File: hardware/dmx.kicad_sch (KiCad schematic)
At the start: 38 parts, among them J101 CORTEX-DEBUG, J102 JAE_DX07S016JA3, SW101 SW_Push, SW102 SW_Push, U101 TPS78433QWDRBRQ1, U102 ATSAMD51G, Y101 32k768

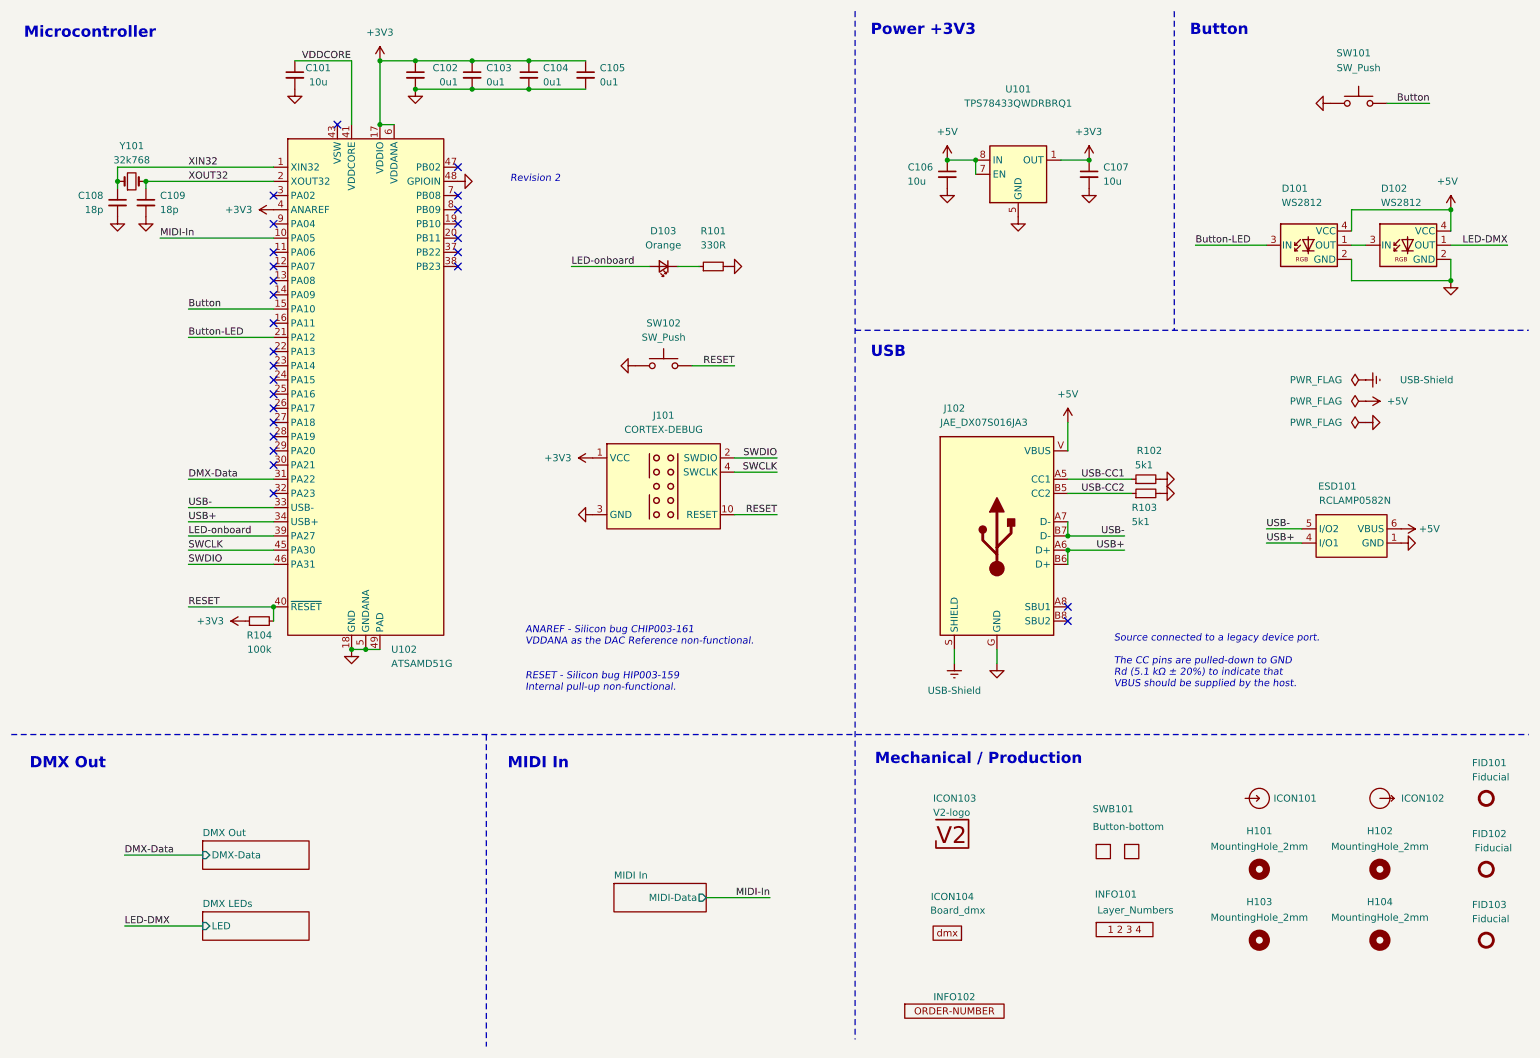
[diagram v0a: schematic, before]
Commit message: Update symbols
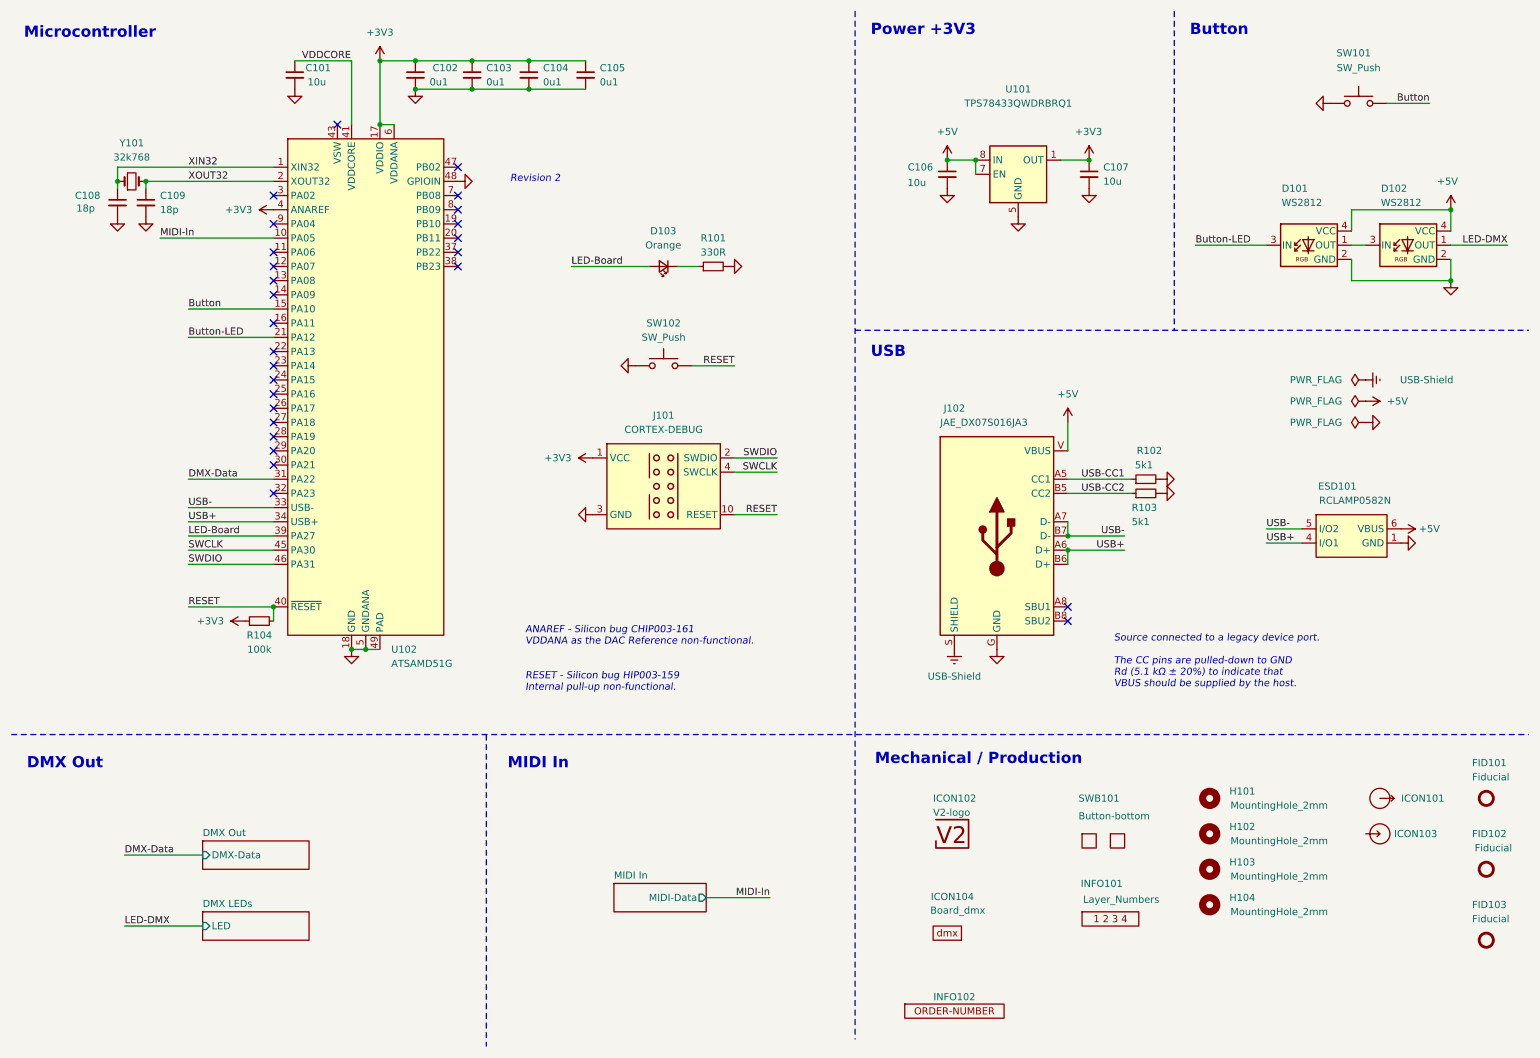
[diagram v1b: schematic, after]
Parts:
- C101: footprint Capacitor_SMD:C_0603_1608Metric -> V2_Capacitor_SMD:C_0603; symbol Device:C_Small -> V2_Device:C_0603_10u; Mouser (none) -> 810-C1608X6S1A106M
- C102, C103, C104, C105: footprint Capacitor_SMD:C_0603_1608Metric -> V2_Capacitor_SMD:C_0603; symbol Device:C_Small -> V2_Device:C_0603_0u1; Mouser (none) -> 810-CGA3E2X7R1H104MA
- C106, C107: footprint Capacitor_SMD:C_0603_1608Metric -> V2_Capacitor_SMD:C_0805; symbol Device:C_Small -> V2_Device:C_0805_10u; Mouser (none) -> 810-C2012X5R1E106K
- C108, C109: footprint Capacitor_SMD:C_0603_1608Metric -> V2_Capacitor_SMD:C_0603; symbol Device:C_Small -> V2_Device:C_0603_18p; Mouser (none) -> 603-CC603JRNPO9BN180
- D103: footprint LED_SMD:LED_0603_1608Metric -> V2_LED:LED_0603; symbol Device:LED_Small -> V2_Device:LED_0603_Orange; Mouser (none) -> 755-SML-D12M8WT86C
- ESD101: Mouser (none) -> 947-RCLAMP0582N.TCT
- J102: Mouser (none) -> 656-DX07S016JA3R1500
- R101: footprint Resistor_SMD:R_0603_1608Metric -> V2_Resistor_SMD:R_0603; symbol Device:R_Small -> V2_Device:R_0603_330R; Mouser (none) -> 71-CRCW0603330RFKEAC
- R102, R103: footprint Resistor_SMD:R_0603_1608Metric -> V2_Resistor_SMD:R_0603; symbol Device:R_Small -> V2_Device:R_0603_5k1; Mouser (none) -> 71-CRCW06035K10FKEAC
- R104: footprint Resistor_SMD:R_0603_1608Metric -> V2_Resistor_SMD:R_0603; symbol Device:R_Small -> V2_Device:R_0603_100k; Mouser (none) -> 71-CRCW0603100KFKEAC
- SW101, SW102: symbol Switch:SW_Push -> V2_Switch:SKSG; Mouser (none) -> 688-SKSGACE010
- U101: Mouser (none) -> 595-TPS78433QWDRBRQ1
- U102: Mouser (none) -> 556-ATSAMD51G19AMU
- Y101: symbol Device:Crystal_Small -> V2_Device:Crystal_3.2x1.5_32k768; Mouser (none) -> 815-ABS0716632.768KT
- renumbered H103 to H102, H102 to H103, ICON102 to ICON101, ICON103 to ICON102, ICON101 to ICON103
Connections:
- net LED-onboard renamed LED-Board
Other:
- moved on the sheet: H101, H102, H103, H104, ICON103, INFO101, SWB101

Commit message: Refresh
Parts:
- C101: Mouser 810-C1608X6S1A106M -> 810-C1608X6S1A106M
- C102, C103, C104, C105: Mouser 810-CGA3E2X7R1H104MA -> 810-CGA3E2X7R1H104MA
- C106, C107: footprint V2_Capacitor_SMD:C_0805 -> V2_Capacitor_SMD:C_0603; Mouser 810-C2012X5R1E106K -> 810-C2012X5R1E106K
- C108, C109: Mouser 603-CC603JRNPO9BN180 -> 603-CC603JRNPO9BN180
- D103: Mouser 755-SML-D12M8WT86C -> 755-SML-D12M8WT86C
- FID101, FID102, FID103: value Fiducial -> Fiducial_Paste
- INFO102: value ORDER-NUMBER -> Order_Number
- J101: value CORTEX-DEBUG -> Cortex_Debug
- J102: value JAE_DX07S016JA3 -> DX07S016JA3; Mouser 656-DX07S016JA3R1500 -> 656-DX07S016JA3R1500
- R101: Mouser 71-CRCW0603330RFKEAC -> 71-CRCW0603330RFKEAC
- R102, R103: Mouser 71-CRCW06035K10FKEAC -> 71-CRCW06035K10FKEAC
- R104: Mouser 71-CRCW0603100KFKEAC -> 71-CRCW0603100KFKEAC
- SW101, SW102: value SW_Push -> SKSG; Mouser 688-SKSGACE010 -> 688-SKSGACE010
- Y101: Mouser 815-ABS0716632.768KT -> 815-ABS0716632.768KT
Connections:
- net USB-Shield renamed Earth
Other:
- moved on the sheet: FID101, FID102, FID103, H101, H102, H103, H104, ICON101, ICON103, INFO101, SWB101

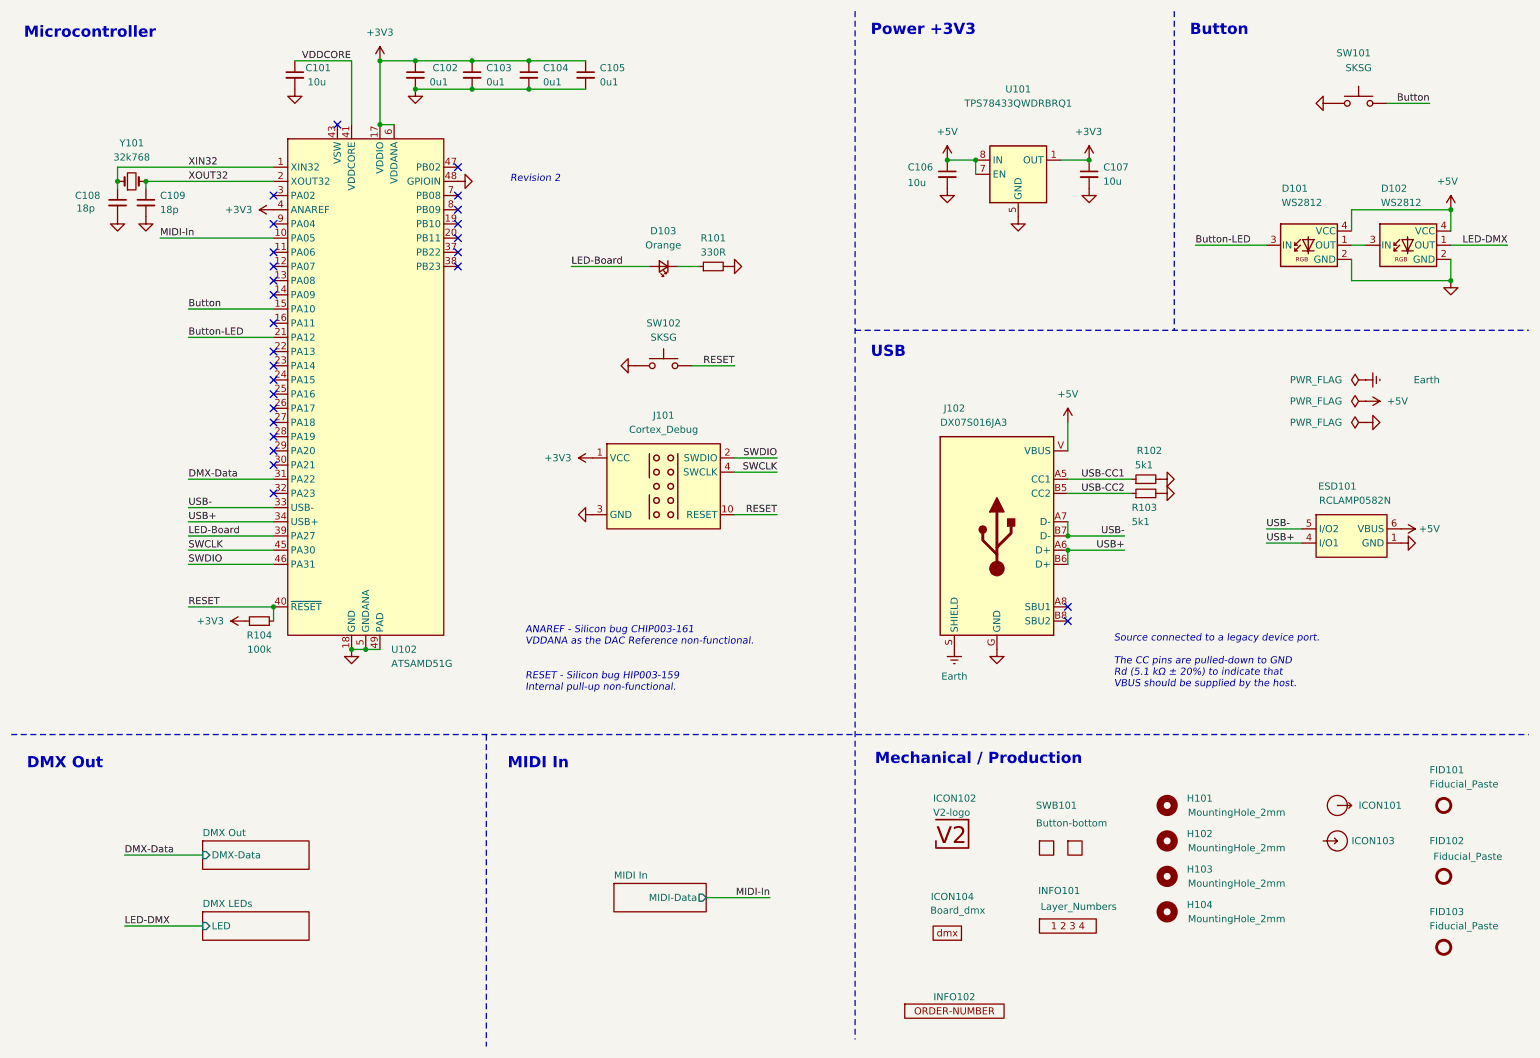
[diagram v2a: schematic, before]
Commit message: Update power symbols
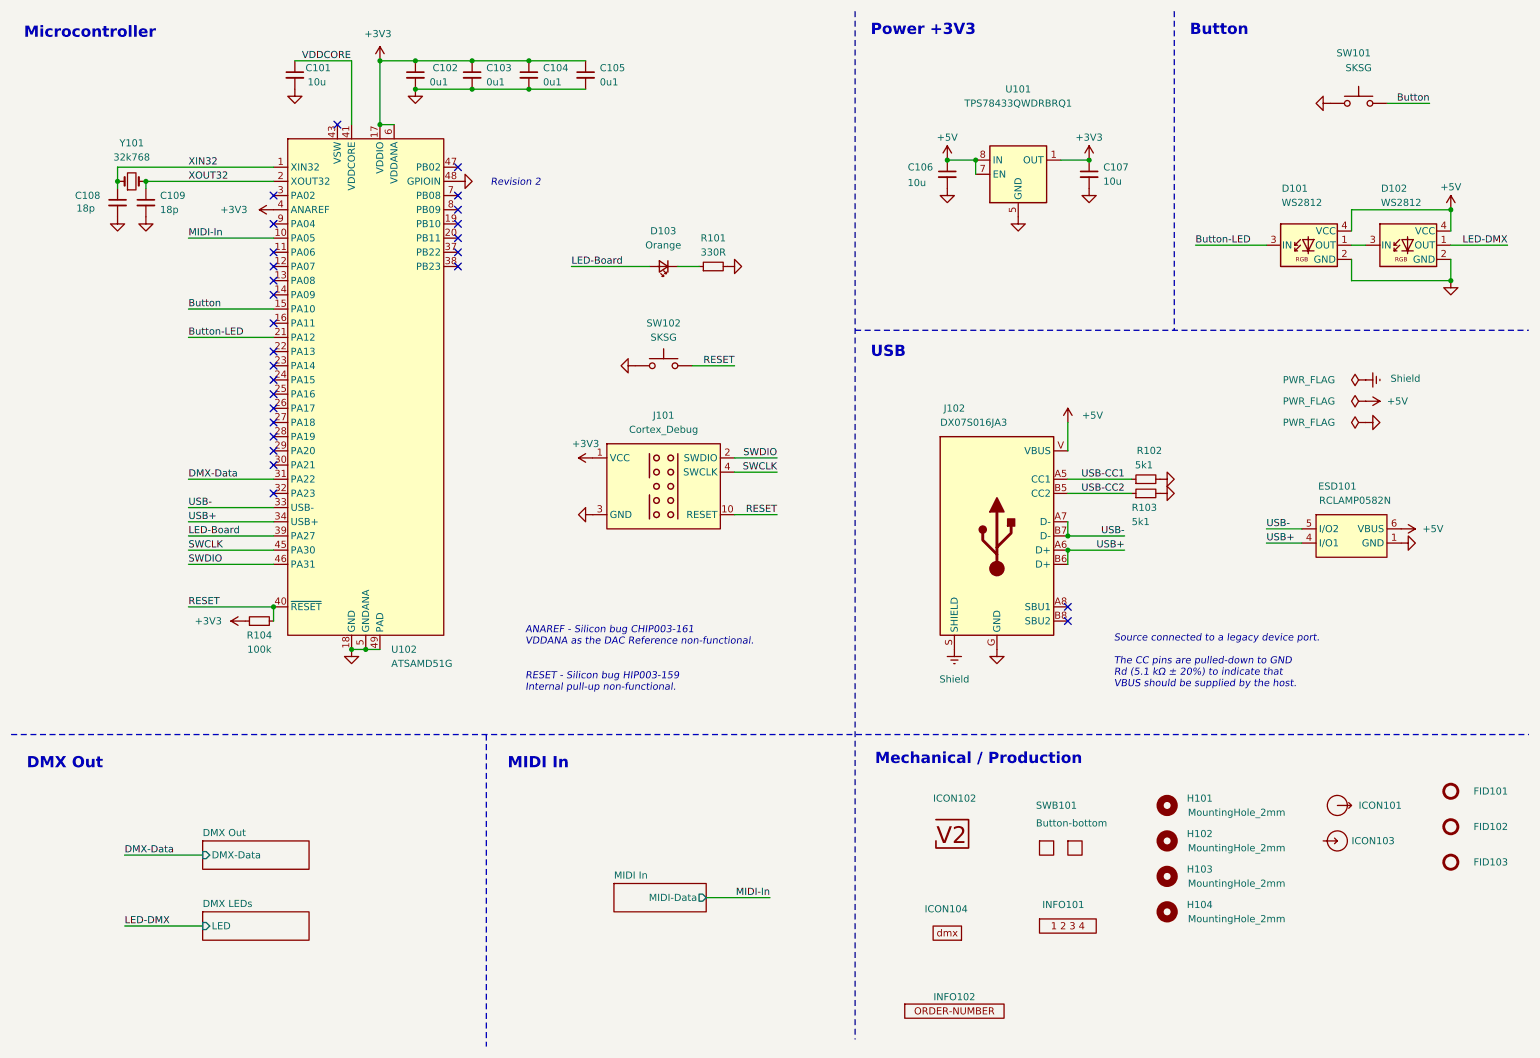
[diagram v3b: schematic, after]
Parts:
- C106, C107: Rating (none) -> 25V
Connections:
- net Earth renamed Shield
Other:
- moved on the sheet: FID101, FID102, FID103

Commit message: Update parts
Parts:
- C101: Manufacturer (none) -> TDK; Product (none) -> C1608X6S1A106M080AC
- C102, C103, C104, C105: Manufacturer (none) -> TDK; Product (none) -> CGA3E2X7R1H104M080AA
- C106, C107: footprint V2_Capacitor_SMD:C_0603 -> V2_Capacitor_SMD:C_0805; Manufacturer (none) -> TDK; Product (none) -> C2012X5R1E106K125AB
- C108, C109: Manufacturer (none) -> YAGEO; Product (none) -> CC0603JRNPO9BN180
- D101, D102: LCSC (none) -> C965555; Manufacturer (none) -> Worldsemi; Product (none) -> WS2812B-2020
- D103: Manufacturer (none) -> ROHM Semiconductor; Product (none) -> SML-D12M8WT86C
- ESD101: Manufacturer (none) -> Semtech; Mouser 947-RCLAMP0582N.TCT -> 947-RCLAMP0582N.TCT; Product (none) -> RCLAMP0582N.TCT
- J102: Manufacturer (none) -> JAE Electronics; Product (none) -> DX07S016JA3R1500
- R101: Manufacturer (none) -> Vishay; Product (none) -> CRCW0603330RFKEAC; Rating (none) -> 100mW
- R102, R103: Manufacturer (none) -> Vishay; Product (none) -> CRCW06035K10FKEAC; Rating (none) -> 100mW
- R104: Manufacturer (none) -> Vishay; Product (none) -> CRCW0603100KFKEAC; Rating (none) -> 100mW
- SW101, SW102: Manufacturer (none) -> Alps Alpine; Product (none) -> SKSGACE010
- U101: Manufacturer (none) -> Texas Instruments; Mouser 595-TPS78433QWDRBRQ1 -> 595-TPS78433QWDRBRQ1; Product (none) -> TPS78433QWDRBRQ1
- U102: Manufacturer (none) -> Microchip Technology; Mouser 556-ATSAMD51G19AMU -> 556-ATSAMD51G19AMU; Product (none) -> ATSAMD51G19A-MU
- Y101: Manufacturer (none) -> ABRACON; Product (none) -> ABS07-166-32.768KHZ-T
